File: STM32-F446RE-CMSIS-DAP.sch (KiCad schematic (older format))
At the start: 43 parts, among them J1 USB_C_Receptacle_USB2.0, J2 Conn_01x04, J3 Conn_02x04_Odd_Even, J4 Conn_02x05_Odd_Even, J5 Conn_01x04_Female, U1 ECMF02-4CMX8, U2 USB3343, U3 AMS1117-1.8, U4 AMS1117-3.3, U5 STM32F446RETx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

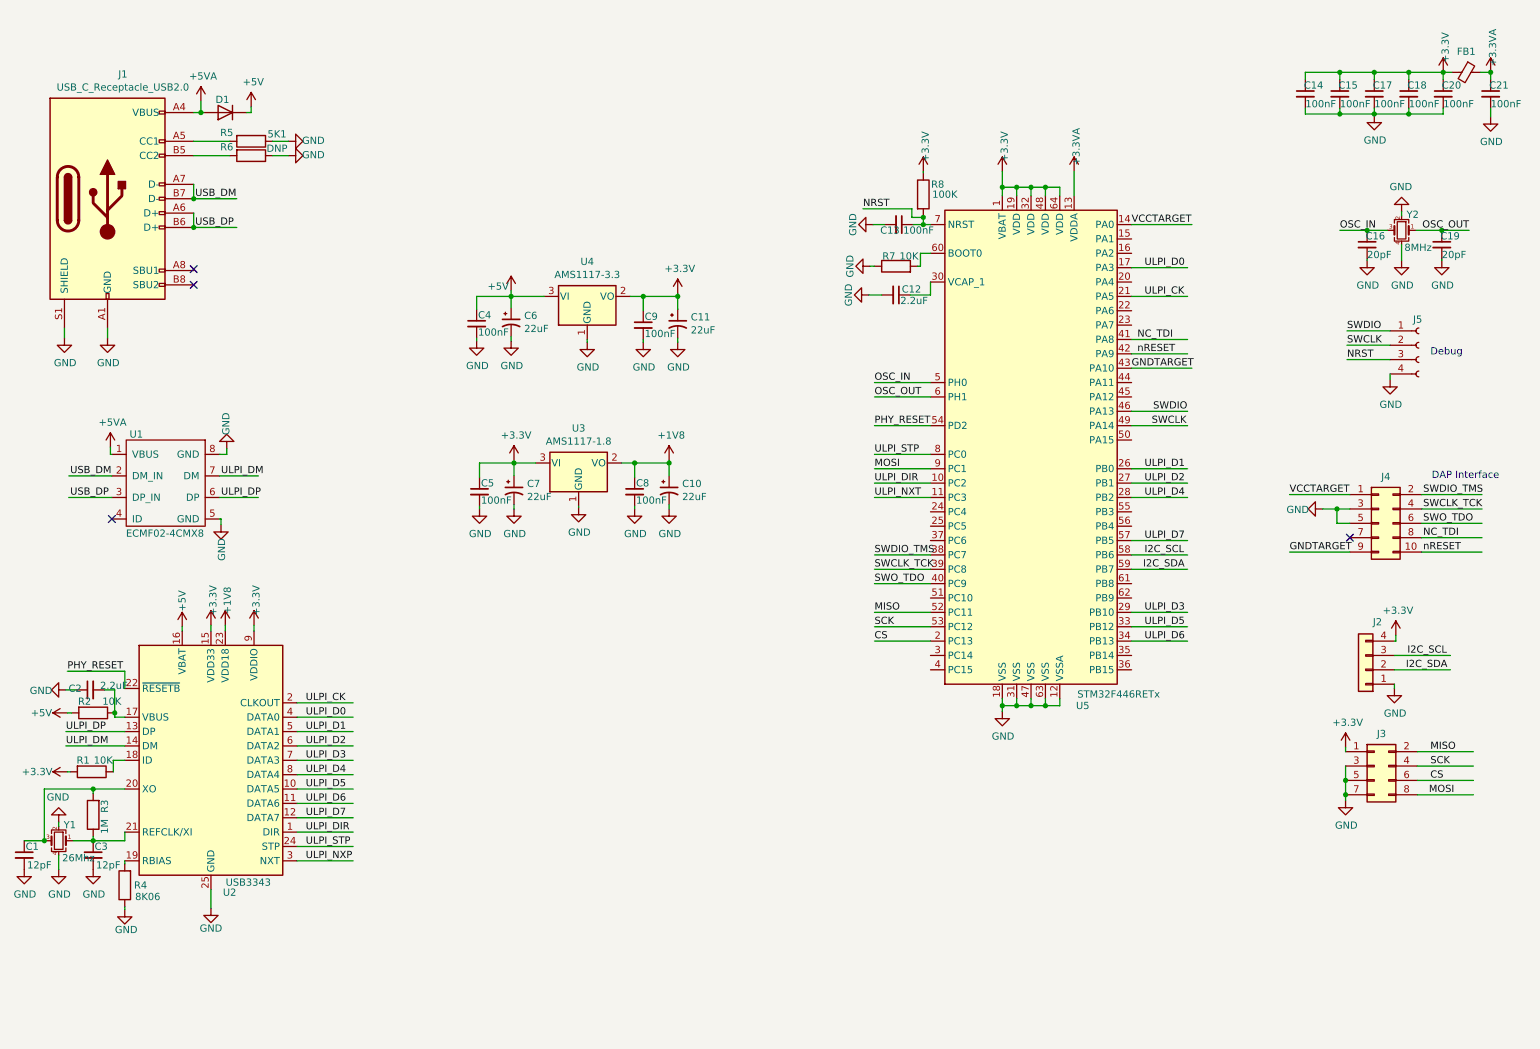
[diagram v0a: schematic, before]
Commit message: update schematic
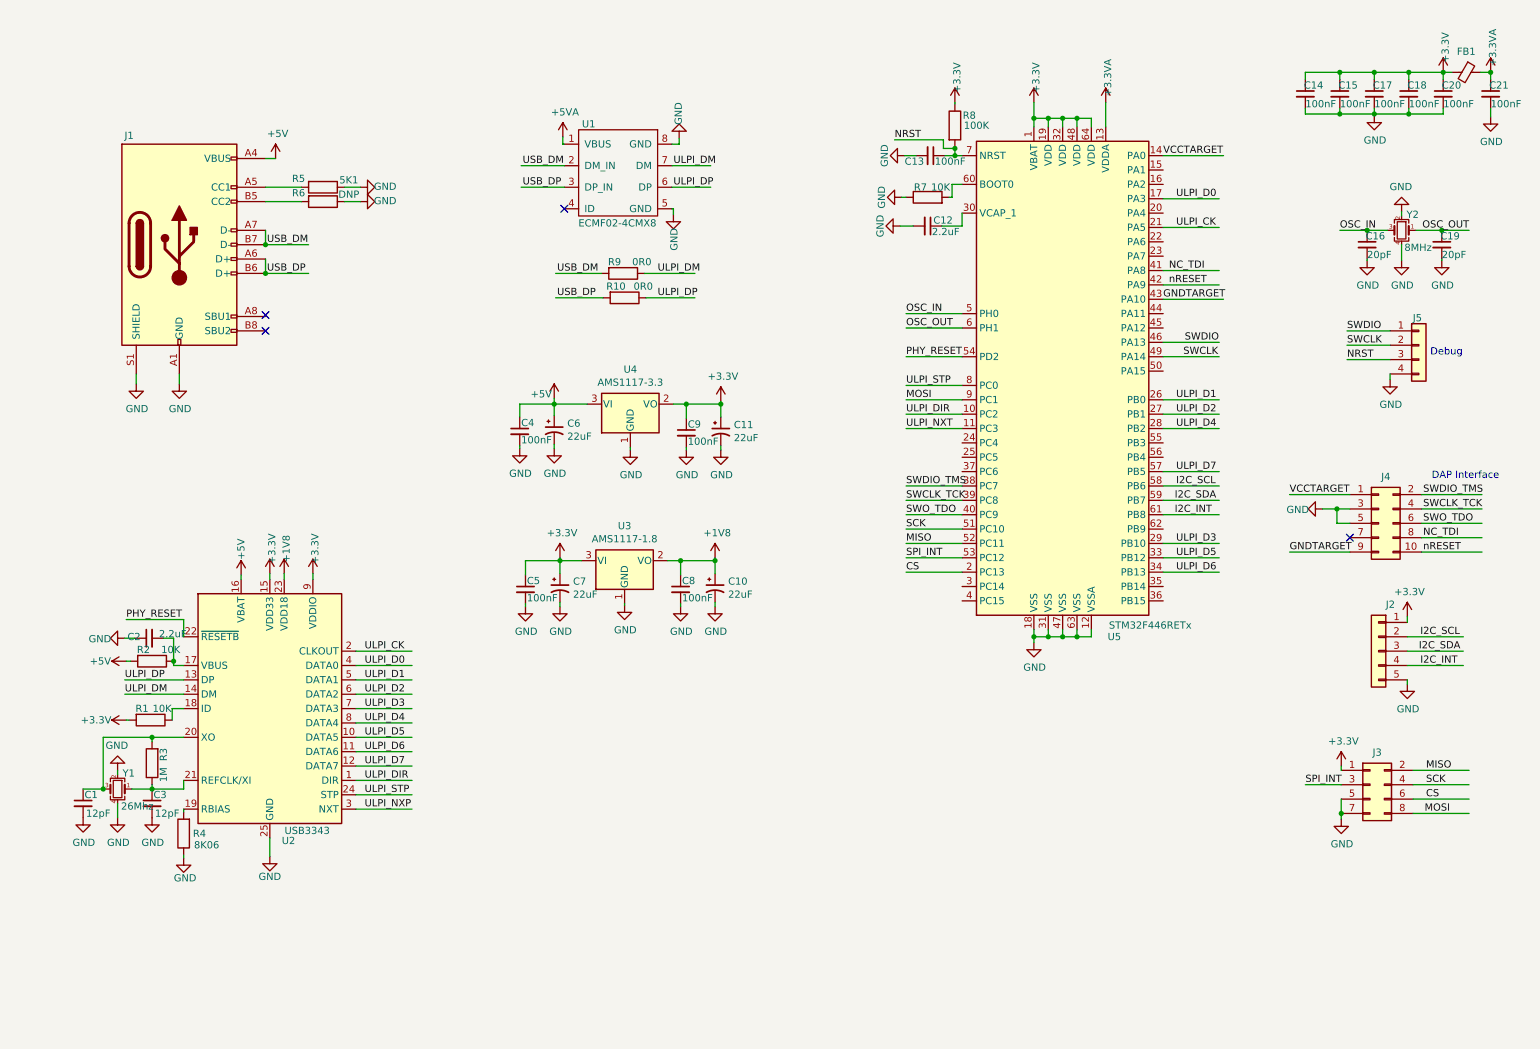
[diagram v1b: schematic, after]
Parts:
- removed D1: 1N4007, Diode_THT:D_DO-41_SOD81_P10.16mm_Horizontal, symbol Diode:1N4007
- removed J2: Conn_01x04, Connector_PinHeader_2.54mm:PinHeader_1x04_P2.54mm_Vertical, symbol Connector_Generic:Conn_01x04
- removed J5: Conn_01x04_Female, Connector_PinHeader_2.54mm:PinHeader_1x04_P2.54mm_Vertical, symbol Connector:Conn_01x04_Female
- added J2: Conn_01x05, Connector_PinHeader_2.54mm:PinHeader_1x05_P2.54mm_Horizontal, symbol Connector_Generic:Conn_01x05
- added J5: Conn_01x04, Connector_PinHeader_2.54mm:PinHeader_1x04_P2.54mm_Horizontal, symbol Connector_Generic:Conn_01x04
- added R10, R9: 0R0, Resistor_SMD:R_0402_1005Metric, symbol Device:R
- C1, C13, C14, C15, C16, C17, C18, C19, C20, C21, C3, C4, C5, C8, C9: footprint Capacitor_SMD:C_0402_1005Metric_Pad0.74x0.62mm_HandSolder -> Capacitor_SMD:C_0603_1608Metric
- C10, C11, C6, C7: footprint Capacitor_SMD:C_0603_1608Metric_Pad1.08x0.95mm_HandSolder -> Capacitor_SMD:C_0805_2012Metric
- C12, C2: footprint Capacitor_SMD:C_0603_1608Metric_Pad1.08x0.95mm_HandSolder -> Capacitor_SMD:C_0603_1608Metric
- FB1: footprint Inductor_SMD:L_0603_1608Metric_Pad1.05x0.95mm_HandSolder -> Inductor_SMD:L_0603_1608Metric
- J1: footprint Connector_USB:USB_C_Receptacle_Amphenol_12401548E4-2A_CircularHoles -> Connector_USB:USB_C_Receptacle_HRO_TYPE-C-31-M-12
- R1, R2, R3, R4, R5, R6, R7, R8: footprint Resistor_SMD:R_0402_1005Metric_Pad0.72x0.64mm_HandSolder -> Resistor_SMD:R_0603_1608Metric
- U1: footprint (none) -> Diode_TVS:Micro_QFN-8_2.5x1.2mm_P0.5mm
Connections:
- net labels added: I2C_INT, SPI_INT
- wire segments 224 -> 226
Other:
- moved on the sheet: C1, C10, C11, C12, C13, C2, C3, C4, C5, C6, C7, C8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

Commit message: Route usb ulpi
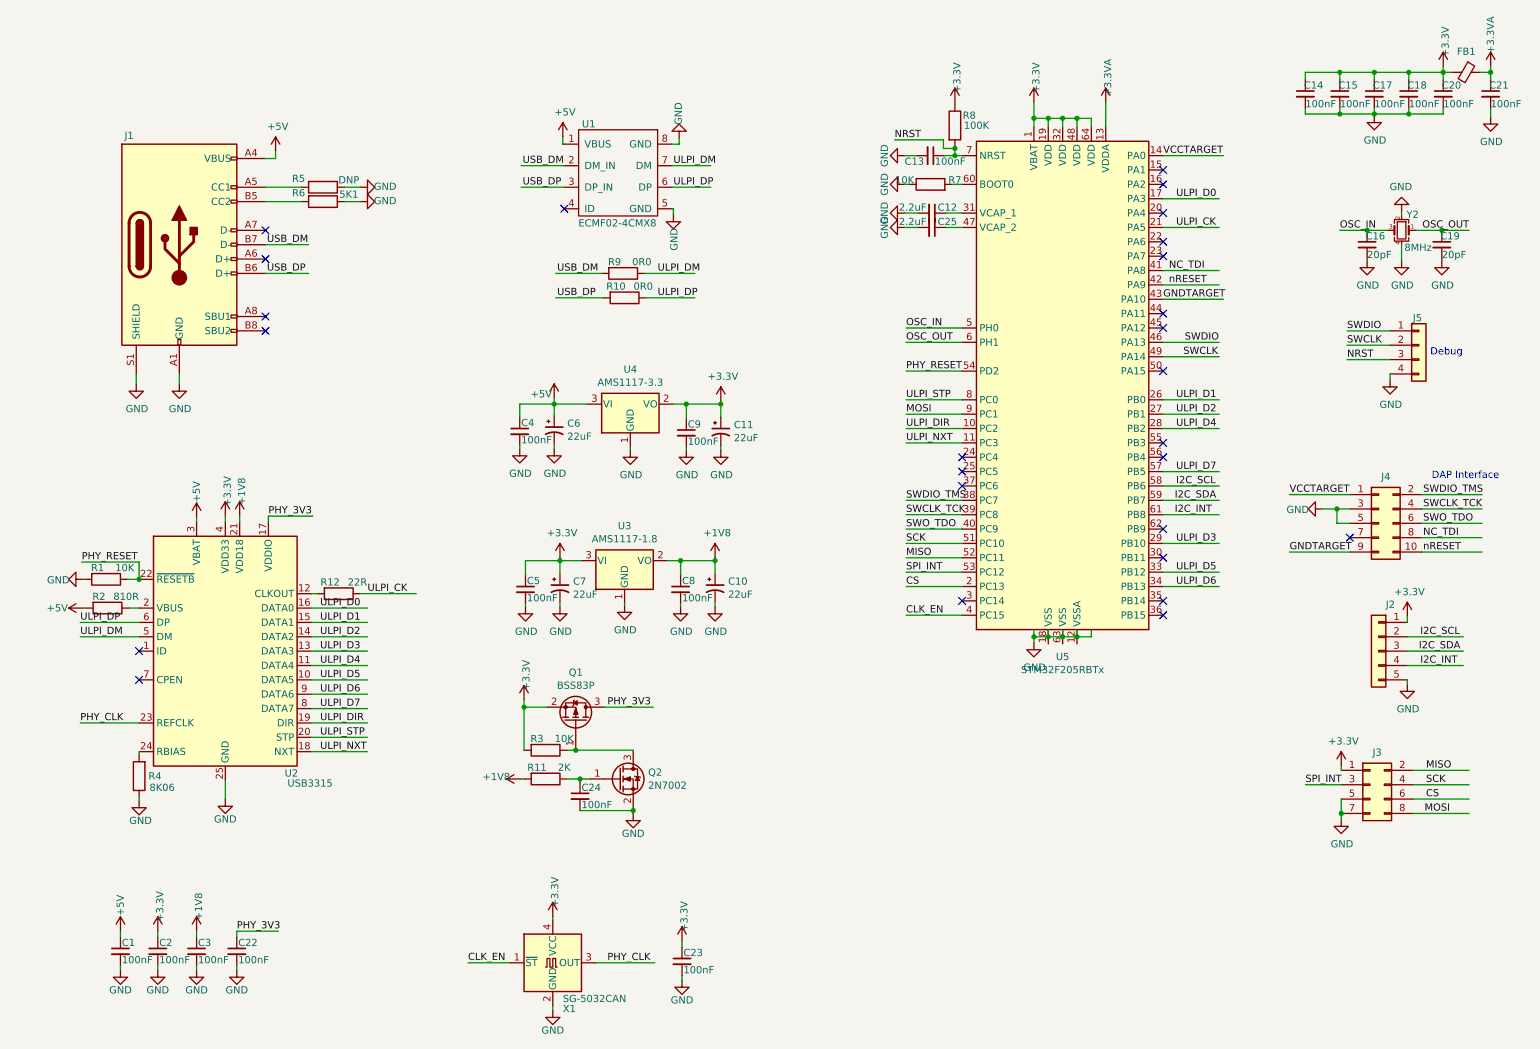
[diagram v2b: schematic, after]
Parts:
- removed U2: USB3343, Package_DFN_QFN:QFN-24-1EP_4x4mm_P0.5mm_EP2.6x2.6mm, symbol Interface_USB:USB3343
- removed U5: STM32F446RETx, Package_QFP:LQFP-64_10x10mm_P0.5mm, symbol MCU_ST_STM32F4:STM32F446RETx
- removed Y1: 26Mhz, Oscillator:Oscillator_SMD_Abracon_ASE-4Pin_3.2x2.5mm, symbol Device:Crystal_GND24_Small
- added C22, C23, C24: 100nF, Capacitor_SMD:C_0603_1608Metric, symbol Device:C_Small
- added C25: 2.2uF, Capacitor_SMD:C_0603_1608Metric, symbol Device:C_Small
- added Q1: BSS83P, Package_TO_SOT_SMD:SOT-23, symbol Transistor_FET:BSS83P
- added Q2: 2N7002, Package_TO_SOT_SMD:SOT-23, symbol Transistor_FET:2N7002
- added R11: 2K, Resistor_SMD:R_0603_1608Metric, symbol Device:R
- added R12: 22R, Resistor_SMD:R_0603_1608Metric, symbol Device:R
- added U2: USB3315, Package_DFN_QFN:QFN-24-1EP_4x4mm_P0.5mm_EP2.6x2.6mm, symbol Interface_USB_Local:USB3315
- added U5: STM32F205RBTx, Package_QFP:LQFP-64_10x10mm_P0.5mm, symbol MCU_ST_STM32F2:STM32F205RBTx
- added X1: SG-5032CAN, Oscillator:Oscillator_SMD_SeikoEpson_SG8002CE-4Pin_3.2x2.5mm, symbol Oscillator:SG-5032CAN
- C1, C3: value 12pF -> 100nF
- C2: value 2.2uF -> 100nF
- R2: value 10K -> 810R
- R3: value 1M -> 10K
- R5: value 5K1 -> DNP
- R6: value DNP -> 5K1
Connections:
- net labels added: CLK_EN, PHY_3V3, PHY_CLK
- net labels removed: +5VA, ULPI_NXP
- wire segments 226 -> 242
- no-connect marks 4 -> 26
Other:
- moved on the sheet: C12, R4, R7

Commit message: update route
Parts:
- removed J5: Conn_01x04, Connector_PinHeader_2.54mm:PinHeader_1x04_P2.54mm_Horizontal, symbol Connector_Generic:Conn_01x04
- added J5: Conn_01x05, Connector_PinHeader_2.54mm:PinHeader_1x05_P2.54mm_Horizontal, symbol Connector_Generic:Conn_01x05
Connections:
- wire segments 242 -> 243
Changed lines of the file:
@@
 L power:GND #PWR049
 U 1 1 6067BCF5
-P 10250 3080
-F 0 "#PWR049" H 10250 2830 50  0001 C CNN
-F 1 "GND" H 10255 2907 50  0000 C CNN
-F 2 "" H 10250 3080 50  0001 C CNN
-F 3 "" H 10250 3080 50  0001 C CNN
-	1    10250 3080
-	1    0    0    -1
-$EndComp
-Wire Wire Line
-	10250 3040 10250 3080
-Wire Wire Line
-	9950 2940 10250 2940
-Wire Wire Line
-	9950 2840 10250 2840
-Wire Wire Line
-	9950 2740 10250 2740
-Text Label 9950 2740 0    50   ~ 0
+P 10240 3330
+F 0 "#PWR049" H 10240 3080 50  0001 C CNN
+F 1 "GND" H 10245 3157 50  0000 C CNN
+F 2 "" H 10240 3330 50  0001 C CNN
+F 3 "" H 10240 3330 50  0001 C CNN
+	1    10240 3330
+	1    0    0    -1
+$EndComp
+Wire Wire Line
+	10240 3290 10240 3330
+Wire Wire Line
+	9940 3190 10240 3190
+Wire Wire Line
+	9940 3090 10240 3090
+Wire Wire Line
+	9940 2990 10240 2990
+Text Label 9940 2990 0    50   ~ 0
 SWDIO
-Text Label 9950 2840 0    50   ~ 0
+Text Label 9940 3090 0    50   ~ 0
 SWCLK
-Text Label 9950 2940 0    50   ~ 0
+Text Label 9940 3190 0    50   ~ 0
 NRST
 Text Label 8820 2820 0    50   ~ 0
@@
 Wire Wire Line
 	10610 2040 10800 2040
-Text Notes 10530 2920 0    50   ~ 0
+Text Notes 10520 3170 0    50   ~ 0
 Debug
 Text Notes 10540 3780 0    50   ~ 0
@@
 Wire Wire Line
 	2420 1540 2490 1540
-$Comp
-L Connector_Generic:Conn_01x04 J5
-U 1 1 606CF531
-P 10450 2840
-F 0 "J5" H 10440 3030 50  0000 C CNN
-F 1 "Conn_01x04" H 10368 2506 50  0001 C CNN
-F 2 "Connector_PinHeader_2.54mm:PinHeader_1x04_P2.54mm_Horizontal" H 10450 2840 50  0001 C CNN
-F 3 "~" H 10450 2840 50  0001 C CNN
-	1    10450 2840
-	1    0    0    -1
-$EndComp
 Text Label 9660 5900 0    50   ~ 0
 SPI_INT
@@
 $EndComp
 NoConn ~ 8670 1620
-NoConn ~ 8670 1720
 NoConn ~ 8670 1920
 NoConn ~ 8670 2120
@@
 	4610 5860 4680 5860
 Wire Wire Line
-	6880 4720 7270 4720
-Text Label 6880 4720 0    50   ~ 0
+	8670 1720 9060 1720
+Text Label 8760 1720 0    50   ~ 0
 CLK_EN
 Text Label 6880 4420 0    50   ~ 0
@@
 NoConn ~ 2420 2240
 NoConn ~ 2420 2040
+$Comp
+L Connector_Generic:Conn_01x05 J5
+U 1 1 60861E42
+P 10440 3090
+F 0 "J5" H 10358 3415 50  0000 C CNN
+F 1 "Conn_01x05" H 10520 3041 50  0001 L CNN
+F 2 "Connector_PinHeader_2.54mm:PinHeader_1x05_P2.54mm_Horizontal" H 10440 3090 50  0001 C CNN
+F 3 "~" H 10440 3090 50  0001 C CNN
+	1    10440 3090
+	1    0    0    1
+$EndComp
+$Comp
+L power:+3.3V #PWR0119
+U 1 1 6088590C
+P 10200 2890
+F 0 "#PWR0119" H 10200 2740 50  0001 C CNN
+F 1 "+3.3V" H 10215 3063 50  0000 C CNN
+F 2 "" H 10200 2890 50  0001 C CNN
+F 3 "" H 10200 2890 50  0001 C CNN
+	1    10200 2890
+	1    0    0    -1
+$EndComp
+Wire Wire Line
+	10200 2890 10240 2890
+NoConn ~ 7270 4720
 $EndSCHEMATC
